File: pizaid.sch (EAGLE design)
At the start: 44 parts, among them X1 S4B-ZR

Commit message: added part info
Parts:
- C1: value (none) -> 22u
- C10, C11, C5: value (none) -> 0.1u
- C2: value (none) -> 2.2u
- C4: value (none) -> 0.22u
- C6, C8: value (none) -> 22u25V
- C7, C9: value (none) -> 22u16V
- L1, L2: value (none) -> 33u
- R1: value (none) -> 100k
- R10, R8: value (none) -> 330
- R12, R13, R2: value (none) -> 10k
- R14, R15, R3: value (none) -> 2.2k
- R4: value (none) -> 0.2
- R5: value (none) -> 24
- R6, R7, R9: value (none) -> 1k
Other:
- note added: "+3.3V"
- note added: "GND"
- note added: "GPIOs"
- note added: "SCL"
- note added: "SDA"
- note added: "Vcc"
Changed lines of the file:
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@@
 <parts>
 <part name="U$1" library="pizaid" deviceset="LT1512" device="CS8"/>
-<part name="R1" library="rcl" deviceset="R-US_" device="R0603"/>
-<part name="R2" library="rcl" deviceset="R-US_" device="R0603"/>
-<part name="R3" library="rcl" deviceset="R-US_" device="R0603"/>
-<part name="R4" library="rcl" deviceset="R-US_" device="0204/7"/>
-<part name="R5" library="rcl" deviceset="R-US_" device="R0603"/>
-<part name="R6" library="rcl" deviceset="R-US_" device="R0603"/>
-<part name="C1" library="rcl" deviceset="C-EU" device="C3225"/>
-<part name="C2" library="rcl" deviceset="C-EU" device="C3216"/>
+<part name="R1" library="rcl" deviceset="R-US_" device="R0603" value="100k"/>
+<part name="R2" library="rcl" deviceset="R-US_" device="R0603" value="10k"/>
+<part name="R3" library="rcl" deviceset="R-US_" device="R0603" value="2.2k"/>
+<part name="R4" library="rcl" deviceset="R-US_" device="0204/7" value="0.2"/>
+<part name="R5" library="rcl" deviceset="R-US_" device="R0603" value="24"/>
+<part name="R6" library="rcl" deviceset="R-US_" device="R0603" value="1k"/>
+<part name="C1" library="rcl" deviceset="C-EU" device="C3225" value="22u"/>
+<part name="C2" library="rcl" deviceset="C-EU" device="C3216" value="2.2u"/>
 <part name="C3" library="rcl" deviceset="C-EU" device="C3225" value="22u"/>
-<part name="C4" library="rcl" deviceset="C-EU" device="C0603"/>
-<part name="C5" library="rcl" deviceset="C-EU" device="C0603"/>
-<part name="L1" library="rcl" deviceset="L-US" device="L5650M"/>
-<part name="L2" library="rcl" deviceset="L-US" device="L5650M"/>
+<part name="C4" library="rcl" deviceset="C-EU" device="C0603" value="0.22u"/>
+<part name="C5" library="rcl" deviceset="C-EU" device="C0603" value="0.1u"/>
+<part name="L1" library="rcl" deviceset="L-US" device="L5650M" value="33u"/>
+<part name="L2" library="rcl" deviceset="L-US" device="L5650M" value="33u"/>
 <part name="GND1" library="supply1" deviceset="GND" device=""/>
 <part name="GND2" library="supply1" deviceset="GND" device=""/>
@@
 <part name="U$6" library="pizaid" deviceset="OKL-T/6" device=""/>
 <part name="U$7" library="pizaid" deviceset="OKL-T/6" device=""/>
-<part name="C6" library="rcl" deviceset="C-EU" device="C3225"/>
-<part name="C7" library="rcl" deviceset="C-EU" device="C3225"/>
-<part name="C8" library="rcl" deviceset="C-EU" device="C3225"/>
-<part name="C9" library="rcl" deviceset="C-EU" device="C3225"/>
+<part name="C6" library="rcl" deviceset="C-EU" device="C3225" value="22u25V"/>
+<part name="C7" library="rcl" deviceset="C-EU" device="C3225" value="22u16V"/>
+<part name="C8" library="rcl" deviceset="C-EU" device="C3225" value="22u25V"/>
+<part name="C9" library="rcl" deviceset="C-EU" device="C3225" value="22u16V"/>
 <part name="GND9" library="supply1" deviceset="GND" device=""/>
 <part name="GND10" library="supply1" deviceset="GND" device=""/>
 <part name="GND11" library="supply1" deviceset="GND" device=""/>
 <part name="GND12" library="supply1" deviceset="GND" device=""/>
-<part name="R7" library="rcl" deviceset="R-US_" device="R0603"/>
-<part name="R8" library="rcl" deviceset="R-US_" device="R0603"/>
+<part name="R7" library="rcl" deviceset="R-US_" device="R0603" value="1k"/>
+<part name="R8" library="rcl" deviceset="R-US_" device="R0603" value="330"/>
 <part name="GND13" library="supply1" deviceset="GND" device=""/>
 <part name="GND14" library="supply1" deviceset="GND" device=""/>
 <part name="GND15" library="supply1" deviceset="GND" device=""/>
 <part name="GND16" library="supply1" deviceset="GND" device=""/>
-<part name="R9" library="rcl" deviceset="R-US_" device="R0603"/>
-<part name="R10" library="rcl" deviceset="R-US_" device="R0603"/>
+<part name="R9" library="rcl" deviceset="R-US_" device="R0603" value="1k"/>
+<part name="R10" library="rcl" deviceset="R-US_" device="R0603" value="330"/>
 <part name="X1" library="con-jst" deviceset="?4B-ZR" device="S"/>
 <part name="R11" library="rcl" deviceset="R-US_" device="R0603"/>
@@
 <part name="GND29" library="supply1" deviceset="GND" device=""/>
 <part name="GND30" library="supply1" deviceset="GND" device=""/>
-<part name="C10" library="rcl" deviceset="C-EU" device="C0603"/>
-<part name="C11" library="rcl" deviceset="C-EU" device="C0603"/>
-<part name="R12" library="rcl" deviceset="R-US_" device="R0603"/>
-<part name="R13" library="rcl" deviceset="R-US_" device="R0603"/>
+<part name="C10" library="rcl" deviceset="C-EU" device="C0603" value="0.1u"/>
+<part name="C11" library="rcl" deviceset="C-EU" device="C0603" value="0.1u"/>
+<part name="R12" library="rcl" deviceset="R-US_" device="R0603" value="10k"/>
+<part name="R13" library="rcl" deviceset="R-US_" device="R0603" value="10k"/>
 <part name="GND31" library="supply1" deviceset="GND" device=""/>
-<part name="R14" library="rcl" deviceset="R-US_" device="R0603"/>
-<part name="R15" library="rcl" deviceset="R-US_" device="R0603"/>
+<part name="R14" library="rcl" deviceset="R-US_" device="R0603" value="2.2k"/>
+<part name="R15" library="rcl" deviceset="R-US_" device="R0603" value="2.2k"/>
 <part name="PCB1" library="pizaid" deviceset="RASPBERRY_PI_B+" device=""/>
 </parts>
@@
 <sheet>
 <plain>
+<text x="374.65" y="-102.87" size="1.778" layer="97">Vcc</text>
+<text x="374.65" y="-105.41" size="1.778" layer="97">+3.3V</text>
+<text x="374.65" y="-107.95" size="1.778" layer="97">GND</text>
+<text x="374.65" y="-113.03" size="1.778" layer="97">SCL</text>
+<text x="374.65" y="-110.49" size="1.778" layer="97">SDA</text>
+<text x="374.65" y="-120.65" size="1.778" layer="97">GPIOs</text>
 </plain>
 <instances>

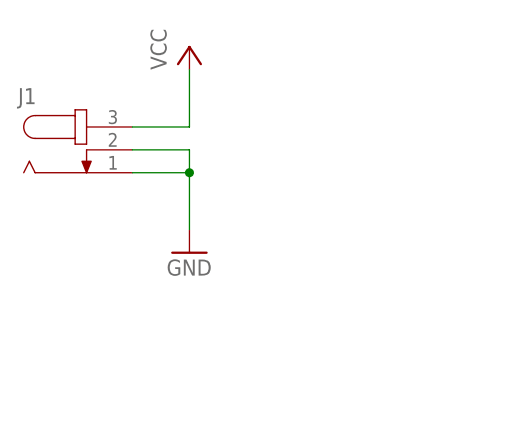
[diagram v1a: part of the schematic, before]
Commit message: changed dcjack
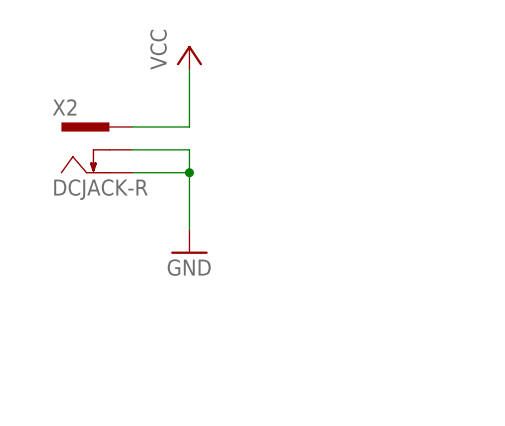
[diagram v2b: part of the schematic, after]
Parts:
- removed J1: (no value), pizaid:JACK-PLUG0
- added X2: DCJACK-R, kamiki-dcjack:DCJACK-R
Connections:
- net GND: now also X2.2, X2.3; no longer J1.1, J1.2
- net VCC: now also X2.1; no longer J1.3
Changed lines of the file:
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@@
 <part name="P+1" library="supply1" deviceset="VCC" device=""/>
 <part name="U$2" library="pizaid" deviceset="SS2040FL" device=""/>
-<part name="J1" library="pizaid" deviceset="JACK-PLUG" device="0"/>
 <part name="P+2" library="supply1" deviceset="VCC" device=""/>
 <part name="GND8" library="supply1" deviceset="GND" device=""/>
@@
 <part name="R15" library="rcl" deviceset="R-US_" device="R0603" value="2.2k"/>
 <part name="PCB1" library="pizaid" deviceset="RASPBERRY_PI_B+" device=""/>
+<part name="X2" library="kamiki-dcjack" deviceset="DCJACK" device="-R"/>
 </parts>
 <sheets>
@@
 <instance part="P+1" gate="VCC" x="36.83" y="102.87"/>
 <instance part="U$2" gate="G$1" x="158.75" y="69.85" rot="R180"/>
-<instance part="J1" gate="G$1" x="-17.78" y="97.79"/>
 <instance part="P+2" gate="VCC" x="-6.35" y="109.22"/>
 <instance part="GND8" gate="1" x="-6.35" y="86.36"/>
@@
 <instance part="R15" gate="G$1" x="242.57" y="-109.22" rot="R90"/>
 <instance part="PCB1" gate="G$1" x="290.83" y="-153.67"/>
+<instance part="X2" gate="G$1" x="-15.24" y="97.79"/>
 </instances>
 <busses>
@@
 </segment>
 <segment>
-<pinref part="J1" gate="G$1" pin="2"/>
 <pinref part="GND8" gate="1" pin="GND"/>
 <wire x1="-12.7" y1="97.79" x2="-6.35" y2="97.79" width="0.1524" layer="91"/>
 <wire x1="-6.35" y1="97.79" x2="-6.35" y2="95.25" width="0.1524" layer="91"/>
-<pinref part="J1" gate="G$1" pin="1"/>
 <wire x1="-6.35" y1="95.25" x2="-6.35" y2="88.9" width="0.1524" layer="91"/>
 <wire x1="-12.7" y1="95.25" x2="-6.35" y2="95.25" width="0.1524" layer="91"/>
 <junction x="-6.35" y="95.25"/>
+<pinref part="X2" gate="G$1" pin="2"/>
+<pinref part="X2" gate="G$1" pin="3"/>
 </segment>
 <segment>
@@
 </segment>
 <segment>
-<pinref part="J1" gate="G$1" pin="3"/>
 <pinref part="P+2" gate="VCC" pin="VCC"/>
 <wire x1="-12.7" y1="100.33" x2="-6.35" y2="100.33" width="0.1524" layer="91"/>
 <wire x1="-6.35" y1="100.33" x2="-6.35" y2="106.68" width="0.1524" layer="91"/>
-</segment>
-<segment>
+<pinref part="X2" gate="G$1" pin="1"/>
+</segment>
+<segment>

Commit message: cleaned board
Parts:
- R11: value (none) -> 10k
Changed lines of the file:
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@@
 <part name="R10" library="rcl" deviceset="R-US_" device="R0603" value="330"/>
 <part name="X1" library="con-jst" deviceset="?4B-ZR" device="S"/>
-<part name="R11" library="rcl" deviceset="R-US_" device="R0603"/>
+<part name="R11" library="rcl" deviceset="R-US_" device="R0603" value="10k"/>
 <part name="GND17" library="supply1" deviceset="GND" device=""/>
 <part name="U$8" library="pizaid" deviceset="B2P-VH" device=""/>
